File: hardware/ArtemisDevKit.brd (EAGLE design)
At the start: 94 x 38.1 mm, 228 parts, among them J2 CORTEX_JTAG_DEBUG_MINIMUM_PTH, J3 CORTEX_JTAG_DEBUG_PTH, J5 1X04_SMD_STRAIGHT_COMBO, J6 QWIIC_RIGHT_ANGLE, J7 CAMERA-HIMAX, J9 1X04_SMD_STRAIGHT_COMBO, U1 DAPLINK_KL26Z, U2 ARTEMIS_MODULESMD, U3 LIS2DH12, U4 AP2127K-1.8V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

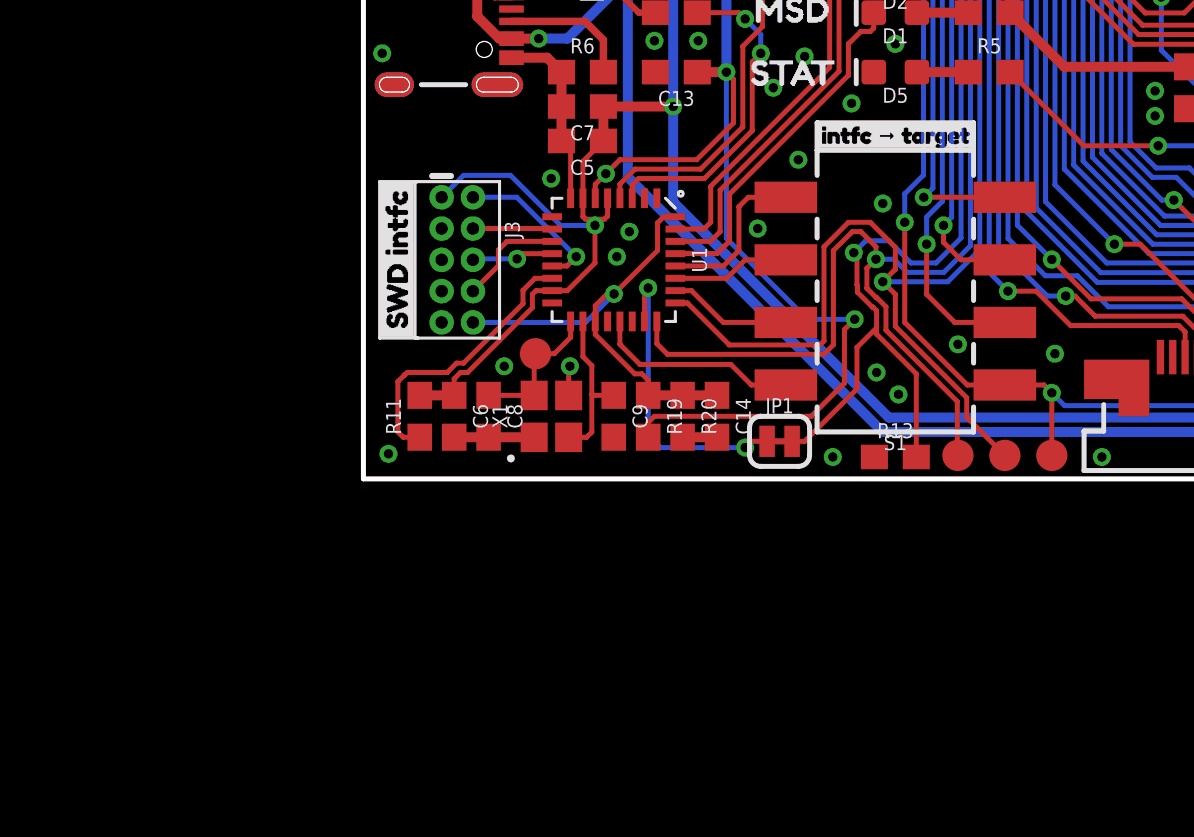
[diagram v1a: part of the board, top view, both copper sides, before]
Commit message: initial changes for v03
- moved Apollo3 reset (TGT_RESET) to TARGET_NRESET on interface chip (pin c1)
- moved TGT_BOOT to pin e30 (pad 9) of the interface chip (still meant to be pulled low most of the time - just making provisions for software control / serial bootloader compatibility later)
- removed test point on clock lines
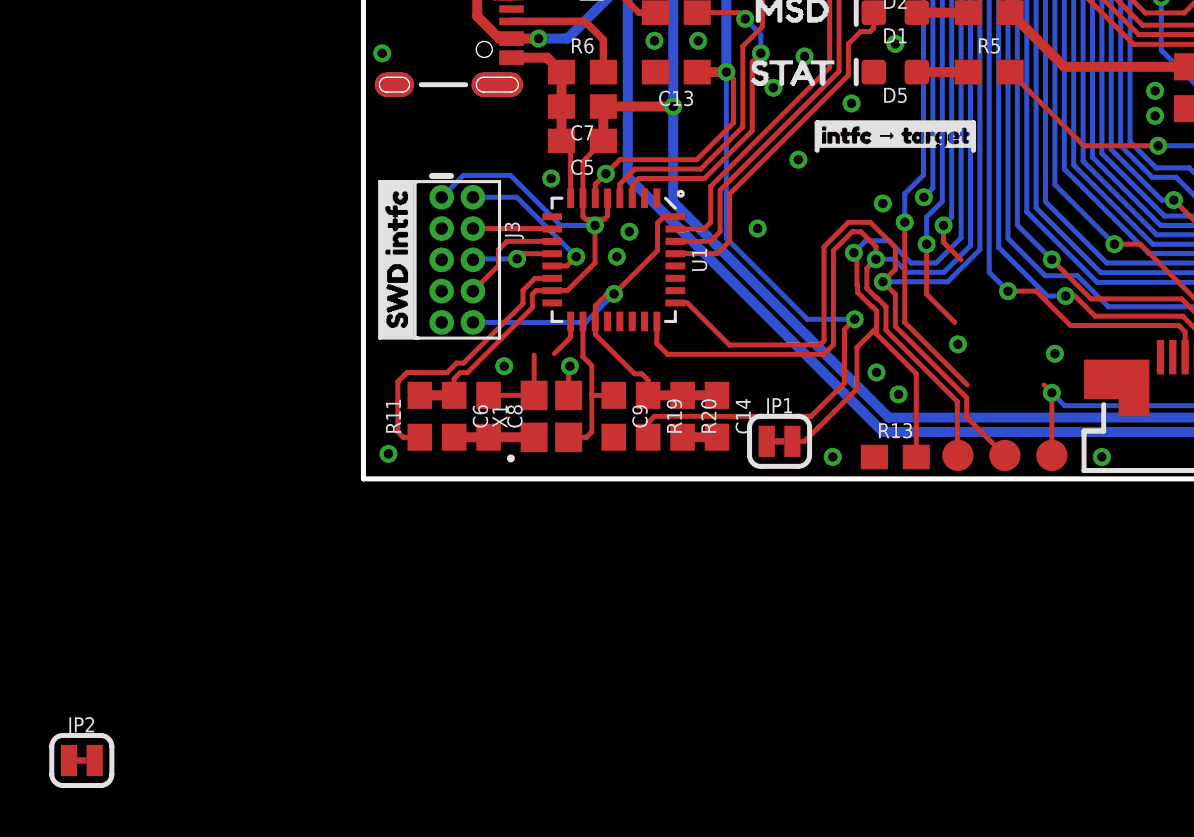
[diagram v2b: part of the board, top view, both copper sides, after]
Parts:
- removed S1: DIP-04SMD, SparkFun-Switches:DIPSWITCH-04-SMD
- removed TP5: (no value), SparkFun-Connectors:PAD.03X.05
- added JP2: JUMPER-SMT_2_NC_TRACE_SILK, SparkFun-Jumpers:SMT-JUMPER_2_NC_TRACE_SILK
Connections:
- net !RST renamed !INTFC_RST
- net TCLK renamed INTFC_SWDCLK
- net TDI renamed INTFC_NC5
- net TDO renamed INTFC_NC6
- net TMS renamed INTFC_SWDIO
- removed net !TGT_RST!_IF: S1.1, U1.21
- removed net N$11: JP1.1, U1.23
- removed net N$17: S1.3, U1.27
- net !TGT_RST: now also U1.22; no longer S1.8
- net N$12: now also JP2.1, U1.26; no longer S1.4, U1.28
- net N$13: no longer TP5.P$1
- net N$18: now also JP1.1, U1.9; no longer S1.2, U1.26
- net TGT_SWCLK: now also JP2.2; no longer S1.7
- net TGT_SWDIO: now also U1.27; no longer S1.6
- net TGT_SWO: now also U1.28; no longer S1.5
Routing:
- net N$11: track 12.5 -> 0.00 mm, vias 2 -> 0
- net !TGT_RST!_IF: track 8.35 -> 0.00 mm
- net N$12: track 6.68 -> 0.00 mm
- net N$18: track 5.02 -> 0.00 mm
- net N$17: track 4.80 -> 0.00 mm
- net TGT_SWO: track 37.3 -> 34.0 mm
- net !TGT_RST: track 127.1 -> 124.0 mm
- net TGT_SWCLK: track 42.2 -> 40.1 mm
- net TGT_SWDIO: track 40.1 -> 38.3 mm
- net N$13: track 5.92 -> 5.08 mm

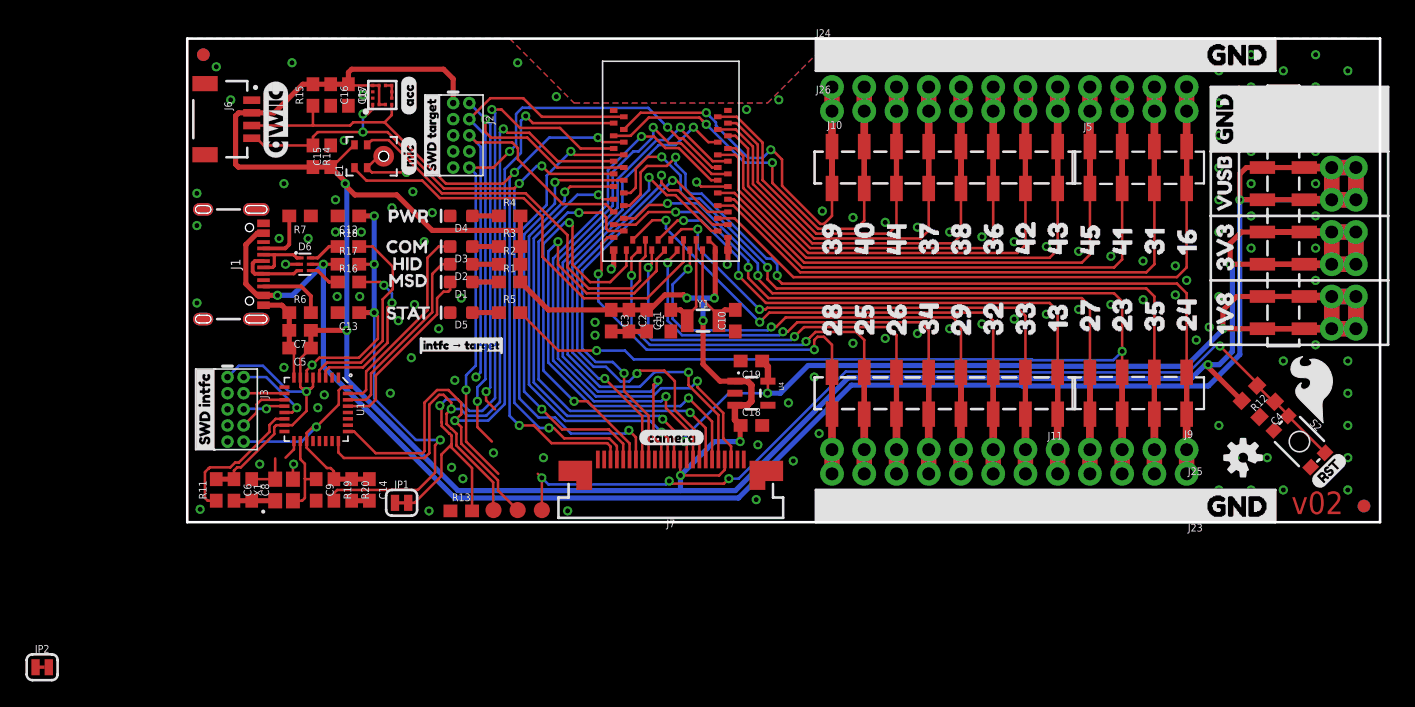
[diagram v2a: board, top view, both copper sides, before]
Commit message: board changes to match initial changes
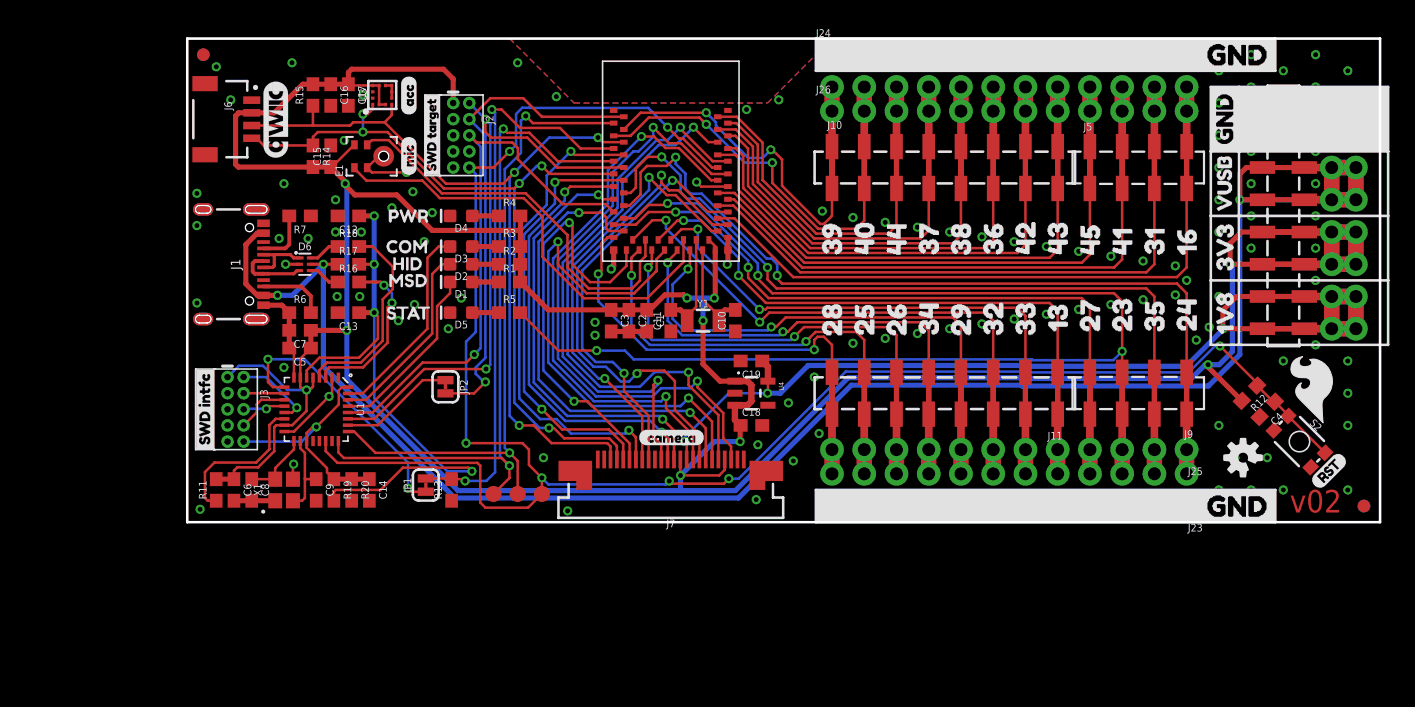
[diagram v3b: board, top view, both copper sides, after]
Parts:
- removed U$38: (no value), 4mar2020_1:INTFC##TARGET12
- TP11, TP3, TP4: value (none) -> TEST-POINT3X5
- moved JP2 38.7 mm to (22.9, 10.7), turned to 270 degrees
- moved JP1 2.36 mm to (21.3, 2.92), turned to 90 degrees
- moved R13 1.82 mm to (23.4, 2.54), turned to 90 degrees
- moved TP11 1.27 mm to (30.5, 2.22)
- moved TP3 1.27 mm to (26.7, 2.22)
- moved TP4 1.27 mm to (28.6, 2.22)
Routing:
- net !TGT_RST: track 124.0 -> 148.4 mm
- net N$18: track 0.00 -> 21.2 mm, vias 0 -> 2
- net TGT_SWO: track 34.0 -> 44.1 mm
- net TGT_BOOT: track 54.7 -> 45.4 mm
- net N$12: track 0.00 -> 9.16 mm
- net TGT_SWDIO: track 38.3 -> 47.4 mm
- net TGT_RX: track 60.1 -> 51.5 mm
- net TGT_TX: track 60.6 -> 54.3 mm
- net GND: track 106.9 -> 111.7 mm, vias 121 -> 111
- net VBUS_IF2: track 45.9 -> 49.9 mm, vias 5 -> 4
- net TGT_SWCLK: track 40.1 -> 38.9 mm
- net N$10: track 11.3 -> 12.1 mm
- net 3.3V: track 281.0 -> 281.7 mm

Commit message: update labels
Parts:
- added U$38: (no value), 29may2020_1:TARGET_BOOT0
- added U$44: (no value), 29may2020_1:TARGET_SWD_CLK1
- U$47: device 4mar2020_1:ARTMBED17 -> 29may2020_1:ARTEMIS_DEV_KIT2
- moved U$47 8.13 mm to (49.4, 2.79)
- moved JP1 3.84 mm to (17.5, 2.41)
- moved JP2 2.96 mm to (19.9, 10.4)
- moved FD3 2.54 mm to (92.7, 1.27)
- moved FD4 2.54 mm to (92.7, 1.27)
- moved J10 2.54 mm to (50.8, 27.9)
- moved J11 2.54 mm to (68.6, 10.2)
- moved J14 2.54 mm to (78.7, 3.81)
- moved J22 2.54 mm to (50.8, 34.3)
- moved J23 2.54 mm to (78.7, 1.27)
- moved J24 2.54 mm to (50.8, 36.8)
- moved J25 2.54 mm to (78.7, 5.71)
- moved J26 2.54 mm to (50.8, 32.4)
- moved J4 2.54 mm to (86.4, 33.0)
- moved J9 2.54 mm to (78.7, 10.2)
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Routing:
- net VBUS_IF2: track 49.9 -> 51.6 mm
- net !TGT_RST: track 148.4 -> 149.9 mm
- net TGT_BOOT: track 45.4 -> 46.8 mm
- net TGT_SWCLK: track 38.9 -> 39.4 mm
- net N$12: track 9.16 -> 8.64 mm

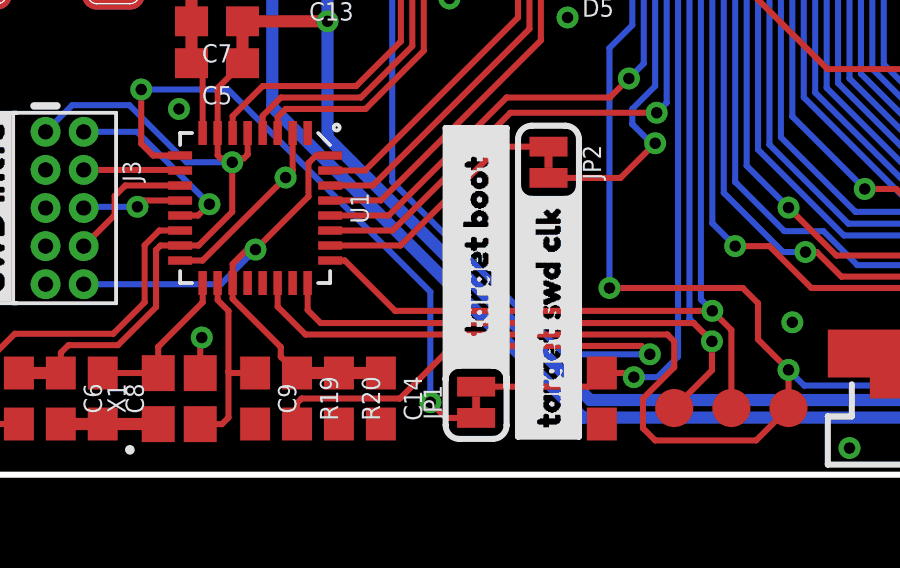
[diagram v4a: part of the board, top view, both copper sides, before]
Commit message: connect PTB1 to PTC1
PTB1 (pin 21 on the 32-pin QFN package) is for 'SW_RESET_BUTTON' in the DAPLink firmware - this is for detecting when the user wants to enter DAPLink maintenance mode
PTC1 (pin 22 on the 32-pin package) is meant to actually control the reset line of the Artemis - this was the mistake that was fixed with a green-wire on the v02 prototype.

The effect of this change is that the user can hold the Artemis reset line while plugging in the DK to enter maintenance mode where they can upgrade the interface firmware, and also that the Artemis will be automatically reset when drag+drop programming occurs
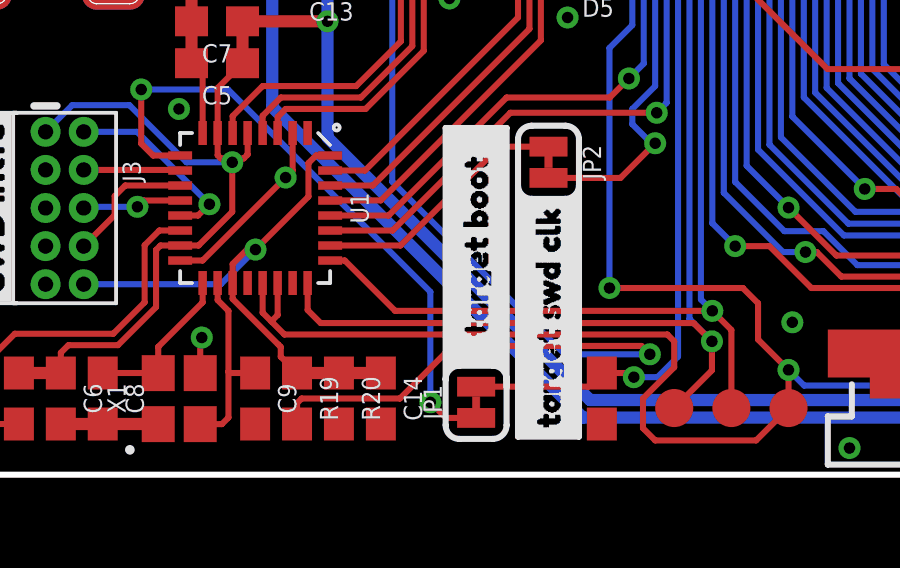
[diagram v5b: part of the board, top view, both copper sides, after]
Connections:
- net !TGT_RST: now also U1.21
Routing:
- net !TGT_RST: track 149.9 -> 151.9 mm
